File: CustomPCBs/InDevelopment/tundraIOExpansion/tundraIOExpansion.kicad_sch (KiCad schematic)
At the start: 58 parts, among them J1 Conn_01x25, J2 Conn_ARM_SWD_TagConnect_TC203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, J3 Conn_ARM_SWD_TagConnect_TC203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, J4 2211SM-04G-B1-TB, J5 2211SM-04G-B1-TB, U1 RP2040, U2 MX25L3233FM2, U4 MX25L3233FM2, U5 RP2040, Y1 12.000MHz, Y2 12.000MHz, Y3 32.768kHz

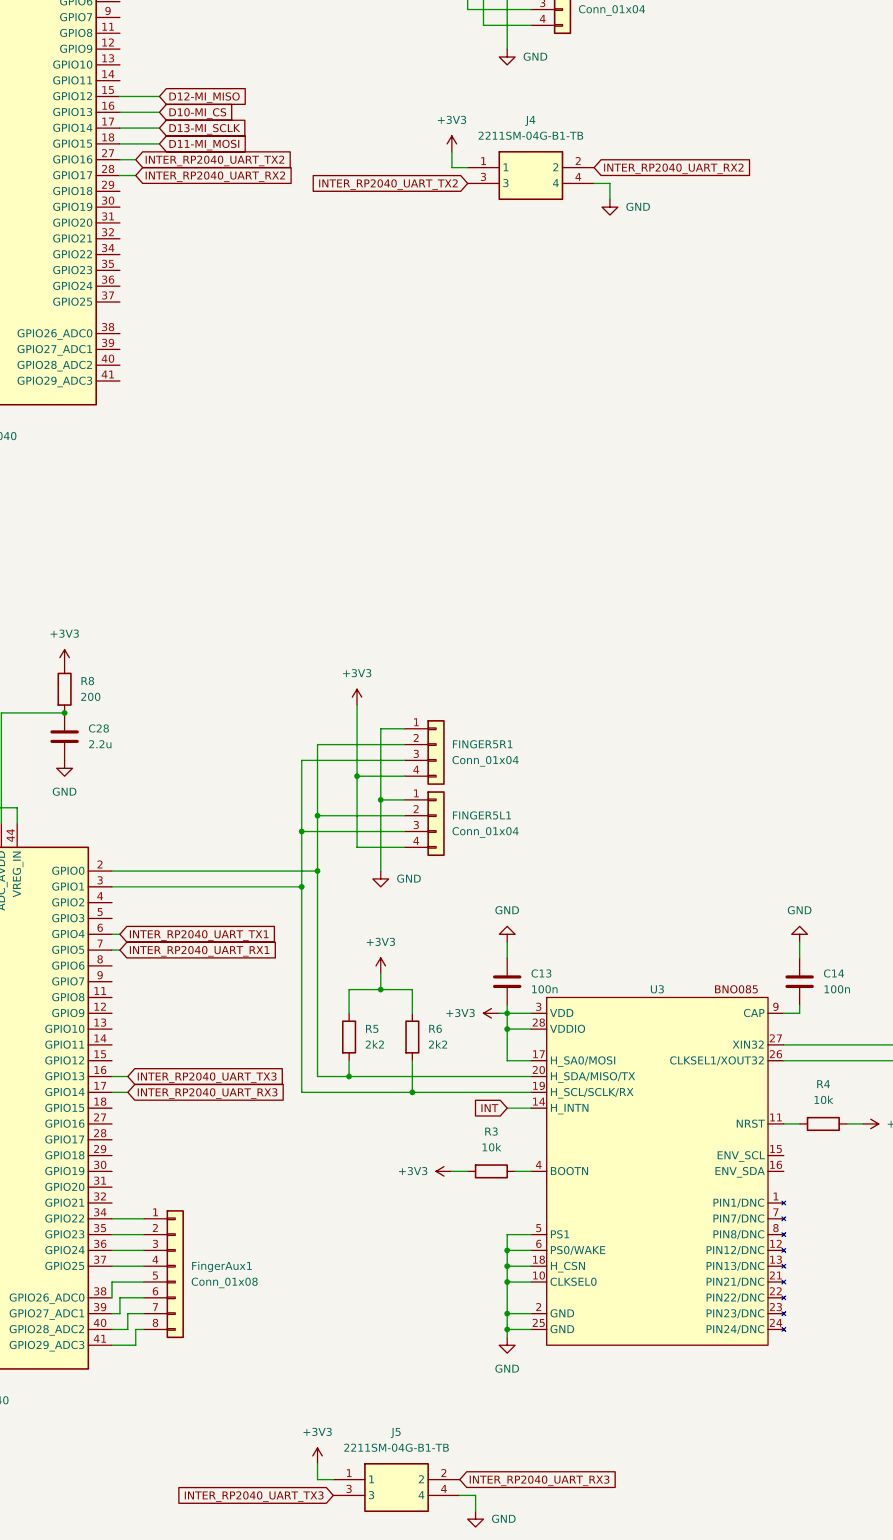
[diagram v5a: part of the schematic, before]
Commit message: Updating components' 3d models for 3d print cases
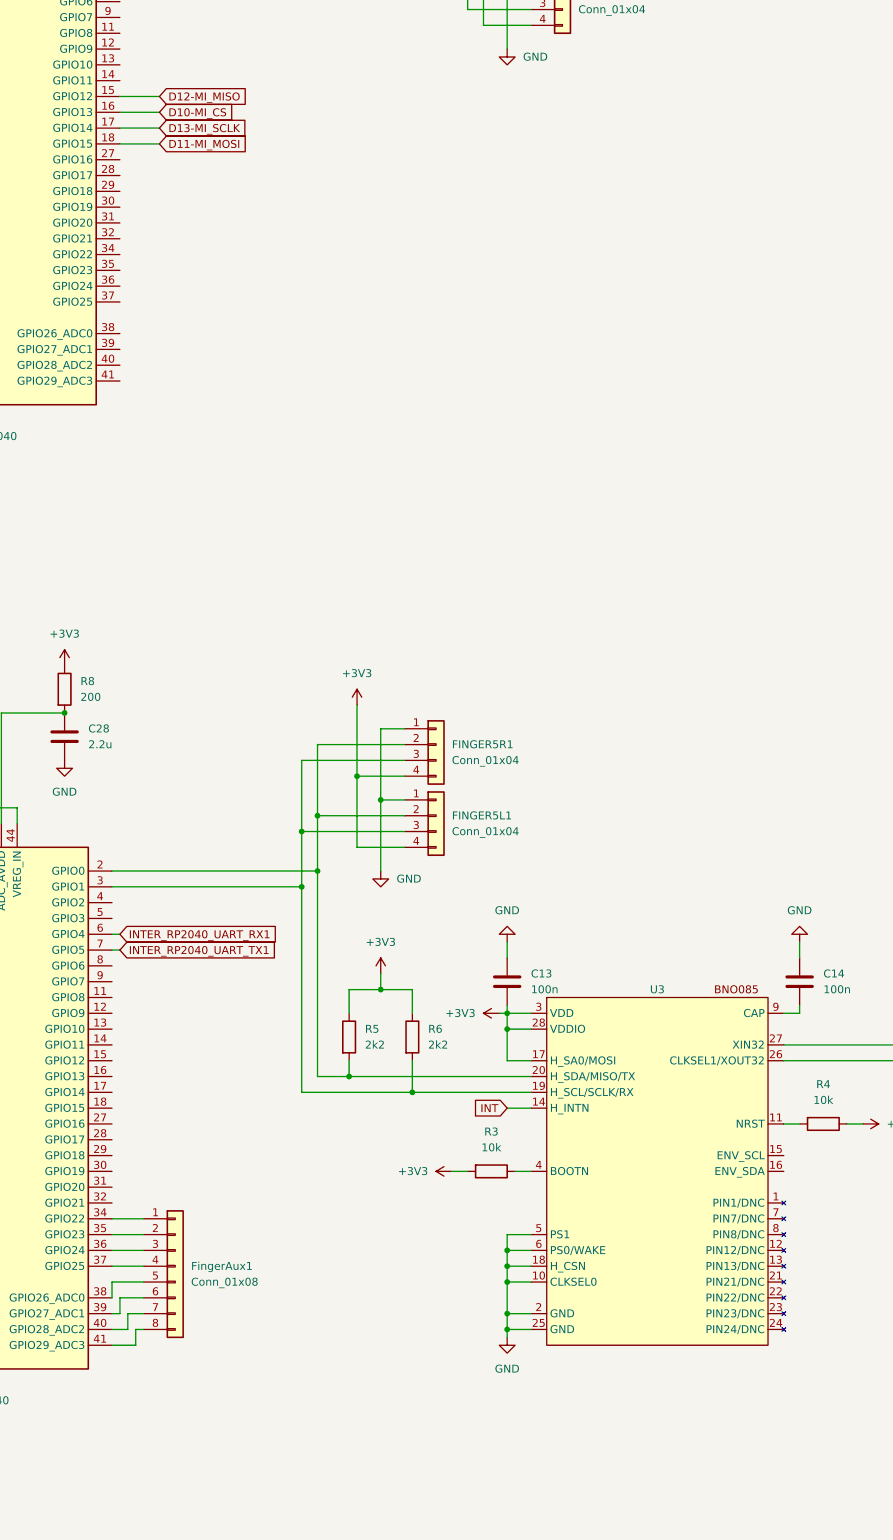
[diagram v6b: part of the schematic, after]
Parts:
- removed J4, J5: 2211SM-04G-B1-TB, Connector_Harting:Harting_har-flexicon_14110413001xxx_1x04-MP_P2.54mm_Vertical, symbol 2211SM-04G-B1-TB:2211SM-04G-B1-TB
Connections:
- net INTER_RP2040_UART_RX1: now also U5.6 (GPIO4); no longer U5.7 (GPIO5)
- net INTER_RP2040_UART_TX1: now also U5.7 (GPIO5); no longer U5.6 (GPIO4)
- net INTER_RP2040_UART_RX2: no longer names the net of U1.28 (GPIO17)
- net INTER_RP2040_UART_RX3: no longer names the net of U5.17 (GPIO14)
- net INTER_RP2040_UART_TX2: no longer names the net of U1.27 (GPIO16)
- net INTER_RP2040_UART_TX3: no longer names the net of U5.16 (GPIO13)

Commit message: tundraIOExpansion ready for DRC
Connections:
- net +1V1: no longer names the net of C7.1, C8.1, C9.1, U1.23 (DVDD), U1.45 (VREG_VOUT), U1.50 (DVDD)
- net +1V1: no longer C23.1, C25.1, C27.1, U5.23 (DVDD), U5.45 (VREG_VOUT), U5.50 (DVDD)
- new net: C23.1, C25.1, C27.1, U5.23 (DVDD), U5.45 (VREG_VOUT), U5.50 (DVDD)
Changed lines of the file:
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@@
-    )
-  )
-  (symbol (lib_id "power:+1V1") (at 154.94 198.12 0) (unit 1)
-    (in_bom yes) (on_board yes) (dnp no) (fields_autoplaced)
-    (property "Reference" "#PWR036" (at 154.94 201.93 0)
-      (effects (font (size 1.27 1.27)) hide)
-    )
-    (property "Value" "+1V1" (at 154.94 193.04 0)
-      (effects (font (size 1.27 1.27)))
-    )
-    (property "Footprint" "" (at 154.94 198.12 0)
-      (effects (font (size 1.27 1.27)) hide)
-    )
-    (property "Datasheet" "" (at 154.94 198.12 0)
-      (effects (font (size 1.27 1.27)) hide)
-    )
-    (pin "1")
-    (instances
-      (project "tundraIOExpansion"
-        (path "/6bc6d498-c151-42bc-9dad-57407f39c6cd"
-          (reference "#PWR036") (unit 1)
-        )
-      )
     )
   )
@@
         )
       )
-    )
-  )
-  (symbol (lib_id "power:+1V1") (at 156.21 43.18 0) (unit 1)
-    (in_bom yes) (on_board yes) (dnp no) (fields_autoplaced)
-    (property "Reference" "#PWR010" (at 156.21 46.99 0)
-      (effects (font (size 1.27 1.27)) hide)
-    )
-    (property "Value" "+1V1" (at 156.21 38.1 0)
-      (effects (font (size 1.27 1.27)))
-    )
-    (property "Footprint" "" (at 156.21 43.18 0)
-      (effects (font (size 1.27 1.27)) hide)
-    )
-    (property "Datasheet" "" (at 156.21 43.18 0)
-      (effects (font (size 1.27 1.27)) hide)
-    )
-    (pin "1")
-    (instances
-      (project "tundraIOExpansion"
-        (path "/6bc6d498-c151-42bc-9dad-57407f39c6cd"
-          (reference "#PWR010") (unit 1)
-        )
-      )

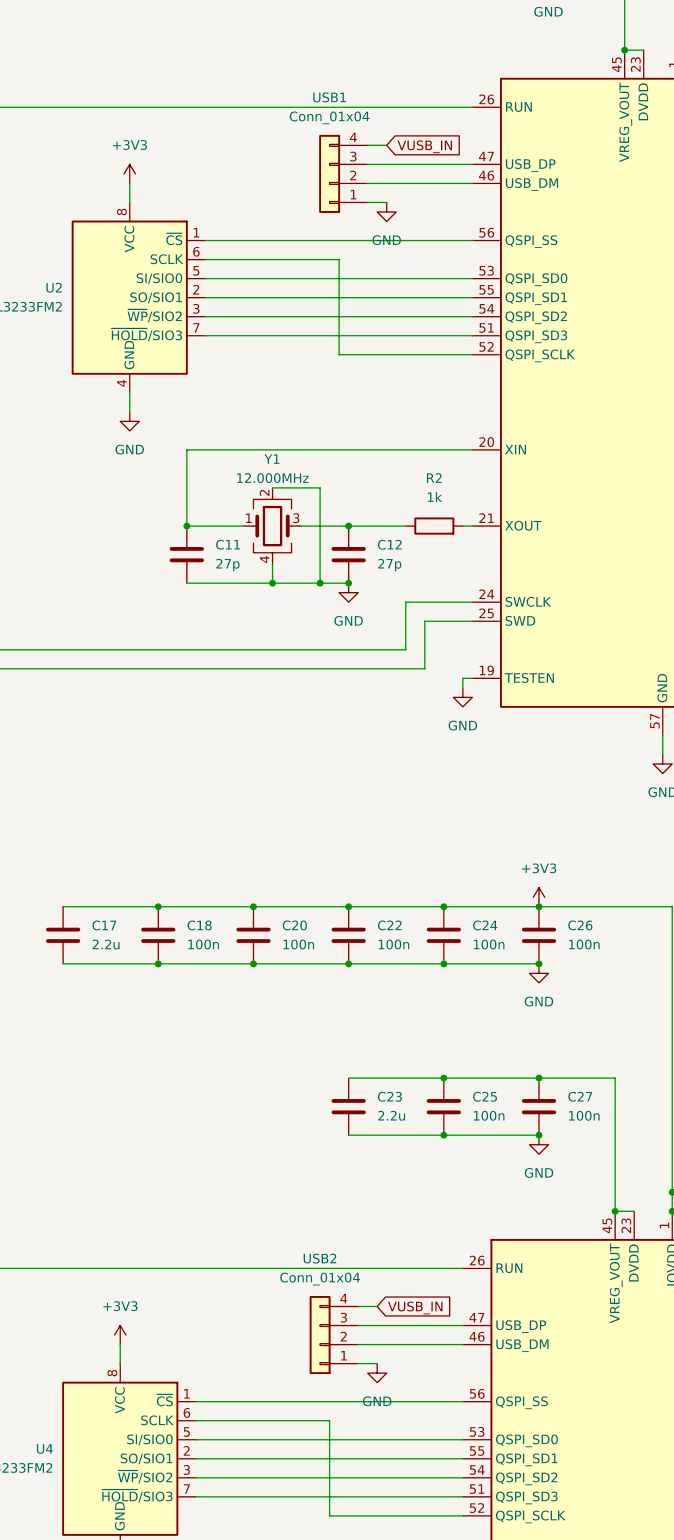
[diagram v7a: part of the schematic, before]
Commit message: Finished tundra expansion board
Had to add a pull up resistor on QSPI_SS on each RP2040 to enable
BOOT_SEL feature when booting with external jumper/button pressed on
USB, to support booting as external flash storage.
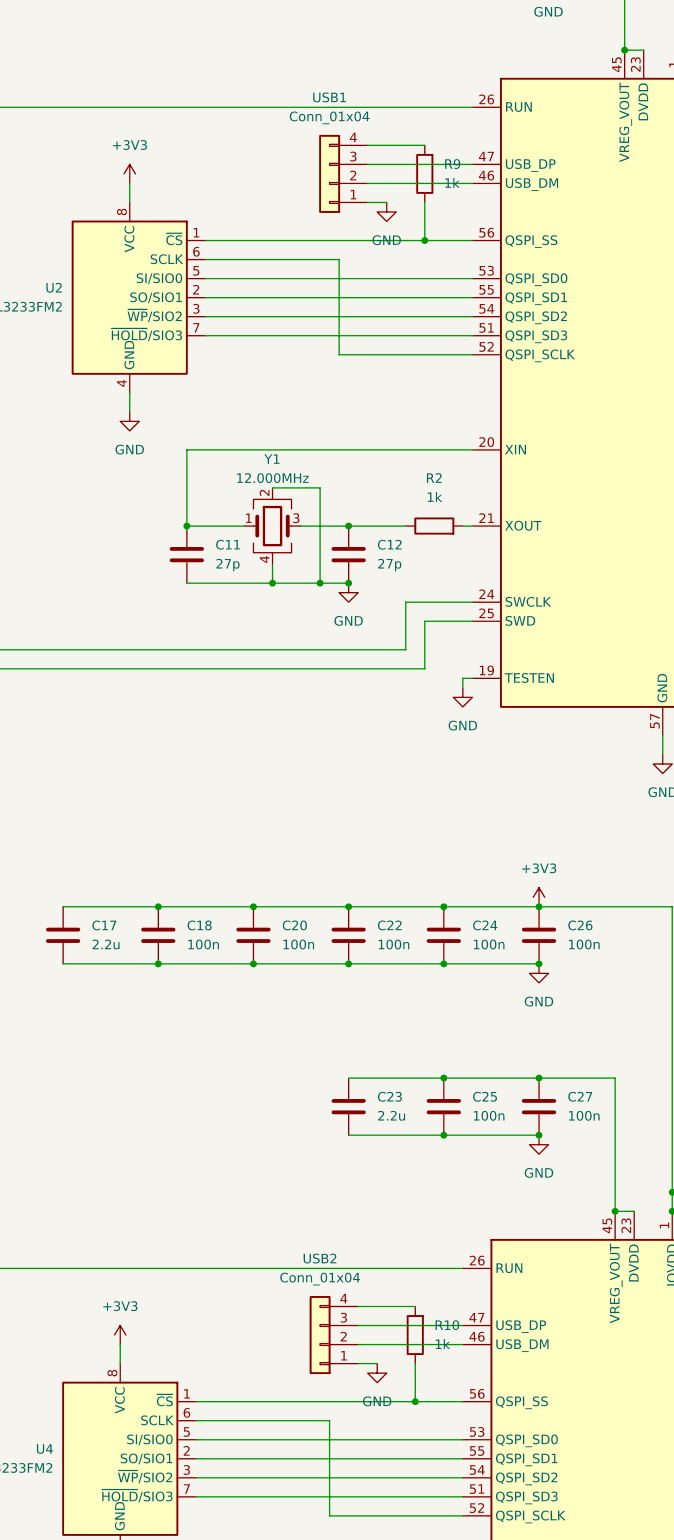
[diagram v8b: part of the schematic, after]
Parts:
- added R10, R9: 1k, Resistor_SMD:R_0402_1005Metric, symbol Device:R
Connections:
- net at U1.56 (QSPI_SS), U2.1 (~{CS}): now also R9.1
- net at U4.1 (~{CS}), U5.56 (QSPI_SS): now also R10.1
- net VUSB_IN: no longer names the net of USB1.4 (Pin_4)
- net VUSB_IN: now also R9.2; no longer USB2.4 (Pin_4)
- new net: R10.2, USB2.4 (Pin_4)
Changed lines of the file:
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@@
   (junction (at 129.54 182.88) (diameter 0) (color 0 0 0 0)
   )
+  (junction (at 138.43 241.3) (diameter 0) (color 0 0 0 0)
+  )
   (junction (at 142.24 205.74) (diameter 0) (color 0 0 0 0)
   )
@@
   (junction (at 187.96 198.12) (diameter 0) (color 0 0 0 0)
   )
+  (junction (at 139.7 86.36) (diameter 0) (color 0 0 0 0)
+  )
   (junction (at 259.08 248.92) (diameter 0) (color 0 0 0 0)
   )
@@
     (stroke (width 0) (type default))
   )
-  (wire (pts (xy 132.08 73.66) (xy 134.62 73.66))
+  (wire (pts (xy 132.08 73.66) (xy 139.7 73.66))
     (stroke (width 0) (type default))
   )
@@
     (stroke (width 0) (type default))
   )
+  (wire (pts (xy 139.7 81.28) (xy 139.7 86.36))
+    (stroke (width 0) (type default))
+  )
   (wire (pts (xy 100.33 78.74) (xy 100.33 81.28))
     (stroke (width 0) (type default))
@@
     (stroke (width 0) (type default))
   )
+  (wire (pts (xy 139.7 86.36) (xy 146.05 86.36))
+    (stroke (width 0) (type default))
+  )
   (wire (pts (xy 255.27 59.69) (xy 255.27 76.2))
     (stroke (width 0) (type default))
@@
     (stroke (width 0) (type default))
   )
-  (wire (pts (xy 130.81 228.6) (xy 133.35 228.6))
+  (wire (pts (xy 130.81 228.6) (xy 138.43 228.6))
     (stroke (width 0) (type default))
   )
@@
     (stroke (width 0) (type default))
   )
+  (wire (pts (xy 138.43 236.22) (xy 138.43 241.3))
+    (stroke (width 0) (type default))
+  )
   (wire (pts (xy 24.13 85.09) (xy 26.67 85.09))
     (stroke (width 0) (type default))
@@
     (stroke (width 0) (type default))
   )
-  (wire (pts (xy 110.49 86.36) (xy 146.05 86.36))
+  (wire (pts (xy 110.49 86.36) (xy 139.7 86.36))
+    (stroke (width 0) (type default))
+  )
+  (wire (pts (xy 138.43 241.3) (xy 144.78 241.3))
     (stroke (width 0) (type default))
   )
-  (wire (pts (xy 109.22 241.3) (xy 144.78 241.3))
+  (wire (pts (xy 109.22 241.3) (xy 138.43 241.3))
     (stroke (width 0) (type default))
   )
@@
     )
   )
-  (global_label "VUSB_IN" (shape input) (at 134.62 73.66 0) (fields_autoplaced)
-    (effects (font (size 1.27 1.27)) (justify left))
-    (property "Intersheetrefs" "${INTERSHEET_REFS}" (at 145.4067 73.66 0)
-      (effects (font (size 1.27 1.27)) (justify left) hide)
-    )
-  )
   (global_label "FPGA_GPIO_13" (shape input) (at 26.67 80.01 0) (fields_autoplaced)
     (effects (font (size 1.27 1.27)) (justify left))
@@
     )
   )
-  (global_label "VUSB_IN" (shape input) (at 133.35 228.6 0) (fields_autoplaced)
-    (effects (font (size 1.27 1.27)) (justify left))
-    (property "Intersheetrefs" "${INTERSHEET_REFS}" (at 144.1367 228.6 0)
-      (effects (font (size 1.27 1.27)) (justify left) hide)
-    )
-  )
   (global_label "D12-MI_MISO" (shape input) (at 203.2 99.06 0) (fields_autoplaced)
     (effects (font (size 1.27 1.27)) (justify left))
@@
     )
   )
+  (symbol (lib_id "Device:R") (at 139.7 77.47 180) (unit 1)
+    (in_bom yes) (on_board yes) (dnp no) (fields_autoplaced)
+    (property "Reference" "R9" (at 142.24 76.2 0)
+      (effects (font (size 1.27 1.27)) (justify right))
+    )
+    (property "Value" "1k" (at 142.24 78.74 0)
+      (effects (font (size 1.27 1.27)) (justify right))
+    )
+    (property "Footprint" "Resistor_SMD:R_0402_1005Metric" (at 141.478 77.47 90)
+      (effects (font (size 1.27 1.27)) hide)
+    )
+    (property "Datasheet" "~" (at 139.7 77.47 0)
+      (effects (font (size 1.27 1.27)) hide)
+    )
+    (pin "1")
+    (pin "2")
+    (instances
+      (project "tundraIOExpansion"
+        (path "/6bc6d498-c151-42bc-9dad-57407f39c6cd"
+          (reference "R9") (unit 1)
+        )
+      )
+    )
+  )
   (symbol (lib_id "Memory_Flash:MX25L3233FM2") (at 100.33 93.98 0) (mirror y) (unit 1)
     (in_bom yes) (on_board yes) (dnp no)
@@
         )
       )
+    )
+  )
+  (symbol (lib_id "Device:R") (at 138.43 232.41 180) (unit 1)
+    (in_bom yes) (on_board yes) (dnp no) (fields_autoplaced)
+    (property "Reference" "R10" (at 140.97 231.14 0)
+      (effects (font (size 1.27 1.27)) (justify right))
+    )
+    (property "Value" "1k" (at 140.97 233.68 0)
+      (effects (font (size 1.27 1.27)) (justify right))
+    )
+    (property "Footprint" "Resistor_SMD:R_0402_1005Metric" (at 140.208 232.41 90)
+      (effects (font (size 1.27 1.27)) hide)
+    )
+    (property "Datasheet" "~" (at 138.43 232.41 0)
+      (effects (font (size 1.27 1.27)) hide)
+    )
+    (pin "1")
+    (pin "2")
+    (instances
+      (project "tundraIOExpansion"
+        (path "/6bc6d498-c151-42bc-9dad-57407f39c6cd"
+          (reference "R10") (unit 1)
+        )
+      )
